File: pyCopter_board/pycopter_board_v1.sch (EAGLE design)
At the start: 36 parts, among them Q1 32.768kHz, U1 BNO055, U3 BMP180

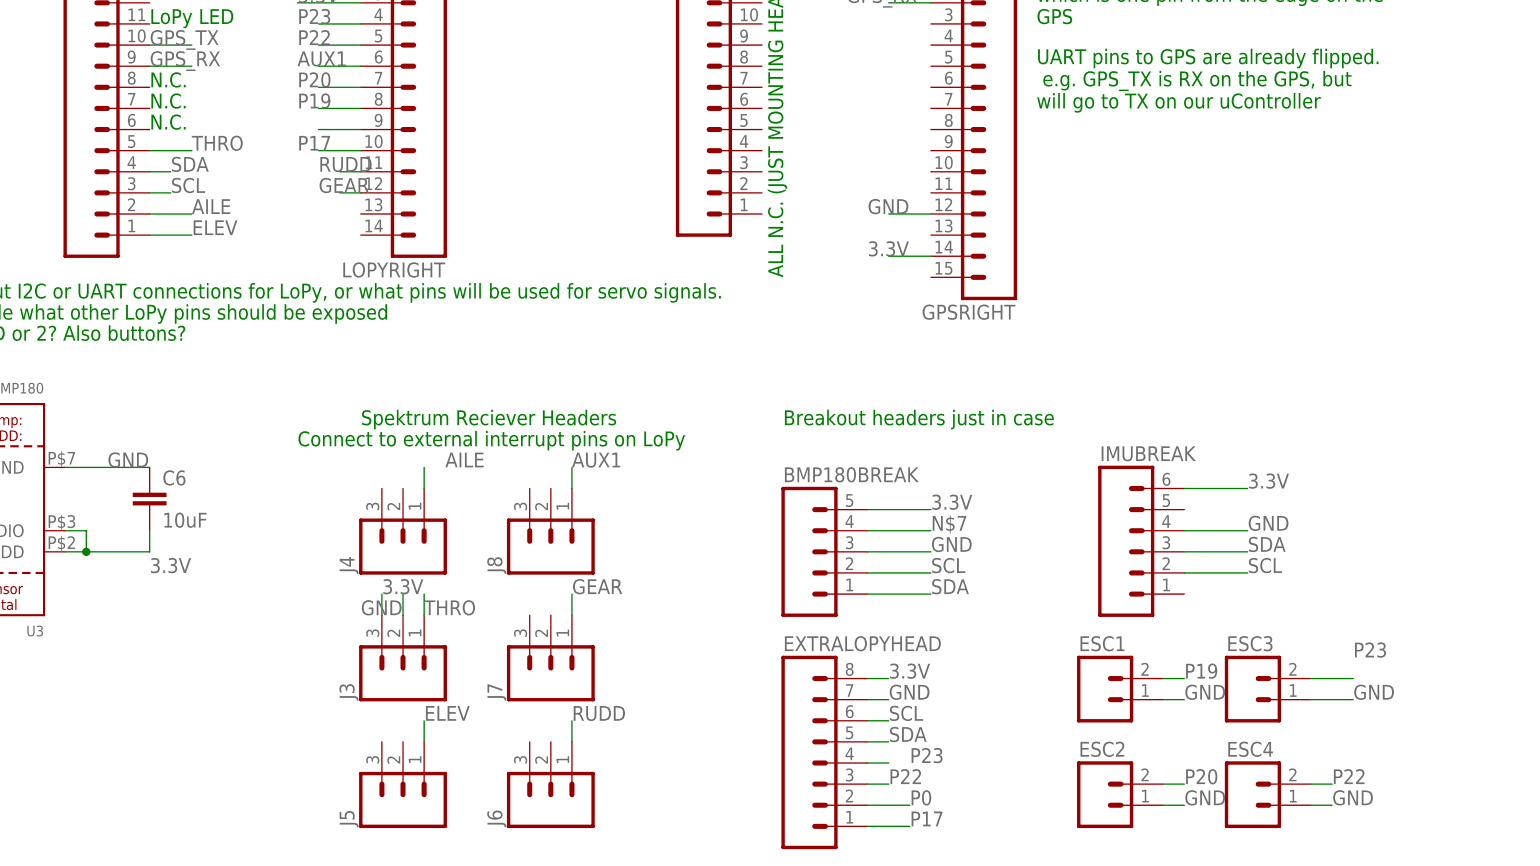
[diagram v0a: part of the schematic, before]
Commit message: added ground plane and made ESCs into triple headers.
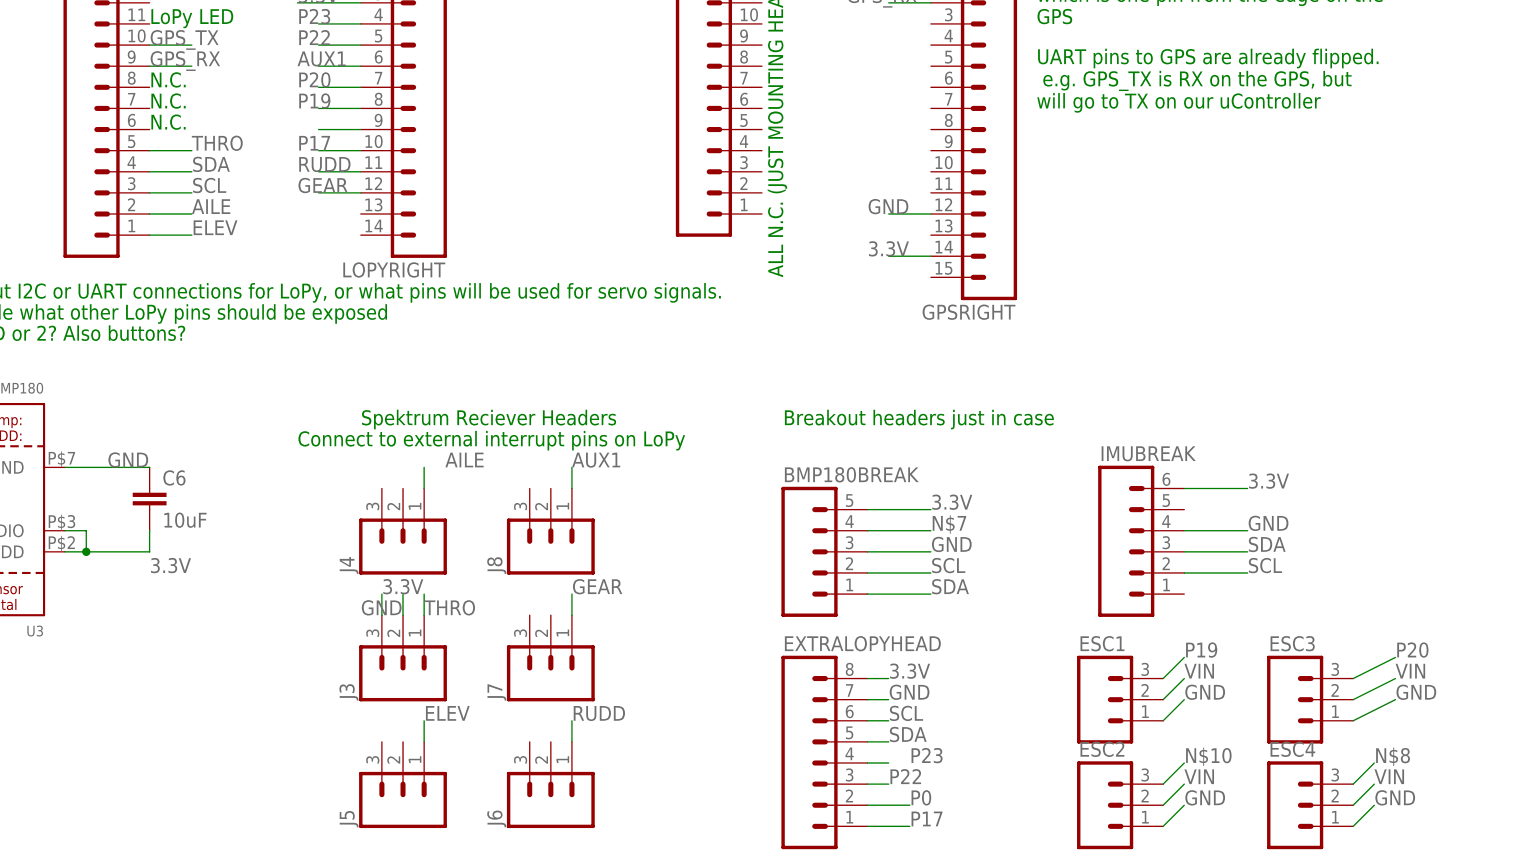
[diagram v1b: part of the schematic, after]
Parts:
- ESC1, ESC2, ESC3, ESC4: device SparkFun-Connectors:M02PTH -> SparkFun-Connectors:M03PTH
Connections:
- new net N$10: ESC2.3
- new net N$8: ESC4.3
- net P19: now also ESC1.3; no longer ESC1.2
- net P20: now also ESC3.3; no longer ESC2.2
- net P22: no longer ESC4.2
- net P23: no longer ESC3.2
- net VIN: now also ESC1.2, ESC2.2, ESC3.2, ESC4.2
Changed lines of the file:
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@@
 <part name="H7" library="holes" deviceset="MOUNT-HOLE" device="3.0"/>
 <part name="H8" library="holes" deviceset="MOUNT-HOLE" device="3.0"/>
-<part name="ESC1" library="SparkFun-Connectors" deviceset="M02" device="PTH"/>
-<part name="ESC2" library="SparkFun-Connectors" deviceset="M02" device="PTH"/>
-<part name="ESC3" library="SparkFun-Connectors" deviceset="M02" device="PTH"/>
-<part name="ESC4" library="SparkFun-Connectors" deviceset="M02" device="PTH"/>
+<part name="ESC1" library="SparkFun-Connectors" deviceset="M03" device="PTH"/>
+<part name="ESC2" library="SparkFun-Connectors" deviceset="M03" device="PTH"/>
+<part name="ESC3" library="SparkFun-Connectors" deviceset="M03" device="PTH"/>
+<part name="ESC4" library="SparkFun-Connectors" deviceset="M03" device="PTH"/>
 </parts>
 <sheets>
@@
 <instance part="H7" gate="G$1" x="-99.06" y="60.96"/>
 <instance part="H8" gate="G$1" x="-93.98" y="50.8"/>
-<instance part="ESC1" gate="G$1" x="175.26" y="-25.4"/>
-<instance part="ESC2" gate="G$1" x="175.26" y="-38.1"/>
-<instance part="ESC3" gate="G$1" x="193.04" y="-25.4"/>
-<instance part="ESC4" gate="G$1" x="193.04" y="-38.1"/>
+<instance part="ESC1" gate="J$1" x="175.26" y="-25.4"/>
+<instance part="ESC2" gate="J$1" x="175.26" y="-38.1"/>
+<instance part="ESC3" gate="J$1" x="198.12" y="-25.4"/>
+<instance part="ESC4" gate="J$1" x="198.12" y="-38.1"/>
 </instances>
 <busses>
@@
 <wire x1="86.36" y1="63.5" x2="78.74" y2="63.5" width="0.1524" layer="91"/>
 <label x="78.74" y="63.5" size="1.778" layer="95"/>
+</segment>
+<segment>
+<pinref part="ESC1" gate="J$1" pin="2"/>
+<wire x1="182.88" y1="-25.4" x2="185.42" y2="-22.86" width="0.1524" layer="91"/>
+<label x="185.42" y="-22.86" size="1.778" layer="95"/>
+</segment>
+<segment>
+<pinref part="ESC3" gate="J$1" pin="2"/>
+<wire x1="205.74" y1="-25.4" x2="210.82" y2="-22.86" width="0.1524" layer="91"/>
+<label x="210.82" y="-22.86" size="1.778" layer="95"/>
+</segment>
+<segment>
+<pinref part="ESC4" gate="J$1" pin="2"/>
+<wire x1="205.74" y1="-38.1" x2="208.28" y2="-35.56" width="0.1524" layer="91"/>
+<label x="208.28" y="-35.56" size="1.778" layer="95"/>
+</segment>
+<segment>
+<pinref part="ESC2" gate="J$1" pin="2"/>
+<wire x1="182.88" y1="-38.1" x2="185.42" y2="-35.56" width="0.1524" layer="91"/>
+<label x="185.42" y="-35.56" size="1.778" layer="95"/>
 </segment>
 </net>
@@
 </segment>
 <segment>
-<pinref part="ESC2" gate="G$1" pin="1"/>
-<wire x1="182.88" y1="-38.1" x2="185.42" y2="-38.1" width="0.1524" layer="91"/>
+<pinref part="ESC2" gate="J$1" pin="1"/>
+<wire x1="182.88" y1="-40.64" x2="185.42" y2="-38.1" width="0.1524" layer="91"/>
 <label x="185.42" y="-38.1" size="1.778" layer="95"/>
 </segment>
 <segment>
-<pinref part="ESC4" gate="G$1" pin="1"/>
-<wire x1="200.66" y1="-38.1" x2="203.2" y2="-38.1" width="0.1524" layer="91"/>
-<label x="203.2" y="-38.1" size="1.778" layer="95"/>
-</segment>
-<segment>
-<pinref part="ESC3" gate="G$1" pin="1"/>
-<wire x1="200.66" y1="-25.4" x2="205.74" y2="-25.4" width="0.1524" layer="91"/>
-<label x="205.74" y="-25.4" size="1.778" layer="95"/>
-</segment>
-<segment>
-<pinref part="ESC1" gate="G$1" pin="1"/>
-<wire x1="182.88" y1="-25.4" x2="185.42" y2="-25.4" width="0.1524" layer="91"/>
+<pinref part="ESC4" gate="J$1" pin="1"/>
+<wire x1="205.74" y1="-40.64" x2="208.28" y2="-38.1" width="0.1524" layer="91"/>
+<label x="208.28" y="-38.1" size="1.778" layer="95"/>
+</segment>
+<segment>
+<pinref part="ESC3" gate="J$1" pin="1"/>
+<wire x1="205.74" y1="-27.94" x2="210.82" y2="-25.4" width="0.1524" layer="91"/>
+<label x="210.82" y="-25.4" size="1.778" layer="95"/>
+</segment>
+<segment>
+<pinref part="ESC1" gate="J$1" pin="1"/>
+<wire x1="182.88" y1="-27.94" x2="185.42" y2="-25.4" width="0.1524" layer="91"/>
 <label x="185.42" y="-25.4" size="1.778" layer="95"/>
 </segment>
@@
 <segment>
 <pinref part="LOPYLEFT" gate="G$1" pin="4"/>
-<wire x1="60.96" y1="38.1" x2="63.5" y2="38.1" width="0.1524" layer="91"/>
-<label x="63.5" y="38.1" size="1.778" layer="95"/>
+<wire x1="60.96" y1="38.1" x2="66.04" y2="38.1" width="0.1524" layer="91"/>
+<label x="66.04" y="38.1" size="1.778" layer="95"/>
 </segment>
 <segment>
@@
 <segment>
 <pinref part="LOPYLEFT" gate="G$1" pin="3"/>
-<wire x1="60.96" y1="35.56" x2="63.5" y2="35.56" width="0.1524" layer="91"/>
-<label x="63.5" y="35.56" size="1.778" layer="95"/>
+<wire x1="60.96" y1="35.56" x2="66.04" y2="35.56" width="0.1524" layer="91"/>
+<label x="66.04" y="35.56" size="1.778" layer="95"/>
 </segment>
 <segment>
@@
 <segment>
 <pinref part="LOPYRIGHT" gate="G$1" pin="11"/>
-<wire x1="86.36" y1="38.1" x2="83.82" y2="38.1" width="0.1524" layer="91"/>
-<label x="81.28" y="38.1" size="1.778" layer="95"/>
+<wire x1="86.36" y1="38.1" x2="81.28" y2="38.1" width="0.1524" layer="91"/>
+<label x="78.74" y="38.1" size="1.778" layer="95"/>
 </segment>
 </net>
@@
 <segment>
 <pinref part="LOPYRIGHT" gate="G$1" pin="12"/>
-<wire x1="86.36" y1="35.56" x2="83.82" y2="35.56" width="0.1524" layer="91"/>
-<label x="81.28" y="35.56" size="1.778" layer="95"/>
+<wire x1="86.36" y1="35.56" x2="81.28" y2="35.56" width="0.1524" layer="91"/>
+<label x="78.74" y="35.56" size="1.778" layer="95"/>
 </segment>
 </net>
@@
 <label x="152.4" y="-33.02" size="1.778" layer="95"/>
 </segment>
-<segment>
-<pinref part="ESC3" gate="G$1" pin="2"/>
-<wire x1="200.66" y1="-22.86" x2="205.74" y2="-22.86" width="0.1524" layer="91"/>
-<label x="205.74" y="-20.32" size="1.778" layer="95"/>
-</segment>
 </net>
 <net name="P22" class="0">
@@
 <label x="149.86" y="-35.56" size="1.778" layer="95"/>
 </segment>
-<segment>
-<pinref part="ESC4" gate="G$1" pin="2"/>
-<wire x1="200.66" y1="-35.56" x2="203.2" y2="-35.56" width="0.1524" layer="91"/>
-<label x="203.2" y="-35.56" size="1.778" layer="95"/>
-</segment>
 </net>
 <net name="P17" class="0">
@@
 </segment>
 <segment>
-<pinref part="ESC2" gate="G$1" pin="2"/>
-<wire x1="182.88" y1="-35.56" x2="185.42" y2="-35.56" width="0.1524" layer="91"/>
-<label x="185.42" y="-35.56" size="1.778" layer="95"/>
+<pinref part="ESC3" gate="J$1" pin="3"/>
+<wire x1="205.74" y1="-22.86" x2="210.82" y2="-20.32" width="0.1524" layer="91"/>
+<label x="210.82" y="-20.32" size="1.778" layer="95"/>
 </segment>
 </net>
@@
 </segment>
 <segment>
-<pinref part="ESC1" gate="G$1" pin="2"/>
-<wire x1="182.88" y1="-22.86" x2="185.42" y2="-22.86" width="0.1524" layer="91"/>
-<label x="185.42" y="-22.86" size="1.778" layer="95"/>
-</segment>
-</net>
+<pinref part="ESC1" gate="J$1" pin="3"/>
+<wire x1="182.88" y1="-22.86" x2="185.42" y2="-20.32" width="0.1524" layer="91"/>
+<label x="185.42" y="-20.32" size="1.778" layer="95"/>
+</segment>
+</net>
+<net name="N$8" class="0">
+<segment>
+<pinref part="ESC4" gate="J$1" pin="3"/>
+<wire x1="205.74" y1="-35.56" x2="208.28" y2="-33.02" width="0.1524" layer="91"/>
+<label x="208.28" y="-33.02" size="1.778" layer="95"/>
+</segment>
+</net>
+<net name="N$10" class="0">
+<segment>
+<pinref part="ESC2" gate="J$1" pin="3"/>
+<wire x1="182.88" y1="-35.56" x2="185.42" y2="-33.02" width="0.1524" layer="91"/>
+<label x="185.42" y="-33.02" size="1.778" layer="95"/>
+</segment>
+</net>

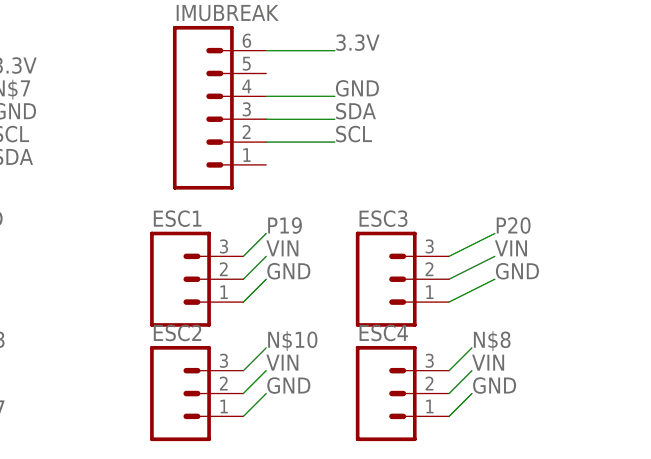
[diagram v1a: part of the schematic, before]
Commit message: started adding traces to board. Added all GND traces and VIN traces. Working on 3.3v now.
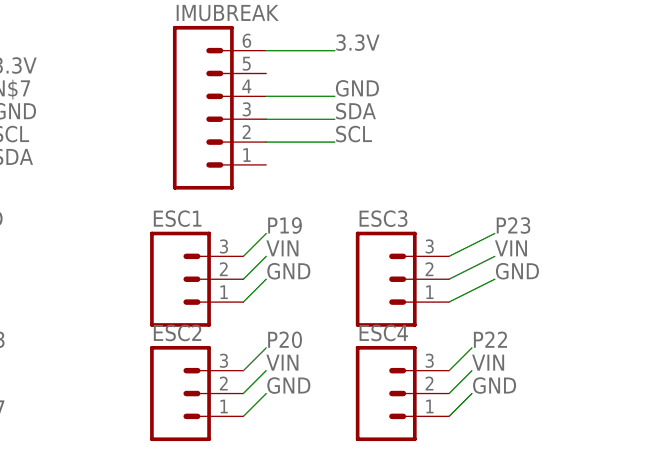
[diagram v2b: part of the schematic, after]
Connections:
- removed net N$10: ESC2.3
- removed net N$8: ESC4.3
- net P20: now also ESC2.3; no longer ESC3.3
- net P22: now also ESC4.3
- net P23: now also ESC3.3
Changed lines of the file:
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@@
 <label x="152.4" y="-33.02" size="1.778" layer="95"/>
+</segment>
+<segment>
+<pinref part="ESC3" gate="J$1" pin="3"/>
+<wire x1="205.74" y1="-22.86" x2="210.82" y2="-20.32" width="0.1524" layer="91"/>
+<label x="210.82" y="-20.32" size="1.778" layer="95"/>
 </segment>
 </net>
@@
 <wire x1="147.32" y1="-35.56" x2="149.86" y2="-35.56" width="0.1524" layer="91"/>
 <label x="149.86" y="-35.56" size="1.778" layer="95"/>
+</segment>
+<segment>
+<pinref part="ESC4" gate="J$1" pin="3"/>
+<wire x1="205.74" y1="-35.56" x2="208.28" y2="-33.02" width="0.1524" layer="91"/>
+<label x="208.28" y="-33.02" size="1.778" layer="95"/>
 </segment>
 </net>
@@
 </segment>
 <segment>
-<pinref part="ESC3" gate="J$1" pin="3"/>
-<wire x1="205.74" y1="-22.86" x2="210.82" y2="-20.32" width="0.1524" layer="91"/>
-<label x="210.82" y="-20.32" size="1.778" layer="95"/>
+<pinref part="ESC2" gate="J$1" pin="3"/>
+<wire x1="182.88" y1="-35.56" x2="185.42" y2="-33.02" width="0.1524" layer="91"/>
+<label x="185.42" y="-33.02" size="1.778" layer="95"/>
 </segment>
 </net>
@@
 </segment>
 </net>
-<net name="N$8" class="0">
-<segment>
-<pinref part="ESC4" gate="J$1" pin="3"/>
-<wire x1="205.74" y1="-35.56" x2="208.28" y2="-33.02" width="0.1524" layer="91"/>
-<label x="208.28" y="-33.02" size="1.778" layer="95"/>
-</segment>
-</net>
-<net name="N$10" class="0">
-<segment>
-<pinref part="ESC2" gate="J$1" pin="3"/>
-<wire x1="182.88" y1="-35.56" x2="185.42" y2="-33.02" width="0.1524" layer="91"/>
-<label x="185.42" y="-33.02" size="1.778" layer="95"/>
-</segment>
-</net>
